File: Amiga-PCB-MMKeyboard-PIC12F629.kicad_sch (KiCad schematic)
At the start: 10 parts, among them J11 Amiga keyboard connector, J12 A500 keyboard connector, J2 PS/2 keyboard connector, U1 PIC12F629-IP

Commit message: v02
- Update PS/2 socket footprint
- Print "values" on silkscreen
- Add 100 nF for PIC
- Shorten "values"
- Move things to the left for more space and to balance the look
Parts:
- added C1: 100nF, Capacitor_SMD:C_0805_2012Metric_Pad1.18x1.45mm_HandSolder, symbol Device:C
- D1: footprint LED_SMD:LED_0805_2012Metric -> LED_SMD:LED_0805_2012Metric_Pad1.15x1.40mm_HandSolder
- D2: value Floppy 0805 -> Drive 0805; footprint LED_SMD:LED_0805_2012Metric -> LED_SMD:LED_0805_2012Metric_Pad1.15x1.40mm_HandSolder
- D3: value Power 2.54 -> Power
- D4: value Floppy 2.54 -> Drive
- J11: value Amiga keyboard connector -> Amiga keyboard
- J12: value A500 keyboard connector -> A500 mainboard
- J2: value PS/2 keyboard connector -> PS/2 keyboard
- R1, R2: footprint Resistor_SMD:R_0805_2012Metric -> Resistor_SMD:R_0805_2012Metric_Pad1.20x1.40mm_HandSolder
- U1: value PIC12F629-IP -> PIC12F629
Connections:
- net GND: now also C1.2
- net VCC: now also C1.1
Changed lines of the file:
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@@
+    )
+  )
+  (global_label "VCC" (shape input) (at 233.68 29.21 180) (fields_autoplaced)
+    (effects (font (size 1.27 1.27)) (justify right))
+    (property "Intersheetrefs" "${INTERSHEET_REFS}" (at 227.0662 29.21 0)
+      (effects (font (size 1.27 1.27)) (justify right) hide)
     )
   )
@@
       (effects (font (size 1.27 1.27)))
     )
-    (property "Value" "Amiga keyboard connector" (at 116.8577 28.7599 0)
+    (property "Value" "Amiga keyboard" (at 116.8577 28.7599 0)
       (effects (font (size 1.27 1.27)))
     )
@@
       (effects (font (size 1.27 1.27)))
     )
-    (property "Value" "PS/2 keyboard connector" (at 204.4877 69.3999 0)
+    (property "Value" "PS/2 keyboard" (at 204.4877 69.3999 0)
       (effects (font (size 1.27 1.27)))
     )
@@
       (effects (font (size 1.27 1.27)))
     )
-    (property "Footprint" "Resistor_SMD:R_0805_2012Metric" (at 144.78 97.028 90)
+    (property "Footprint" "Resistor_SMD:R_0805_2012Metric_Pad1.20x1.40mm_HandSolder" (at 144.78 97.028 90)
       (effects (font (size 1.27 1.27)) hide)
     )
@@
       (effects (font (size 1.27 1.27)) (justify left))
     )
-    (property "Value" "PIC12F629-IP" (at 181.2641 30.0299 0)
+    (property "Value" "PIC12F629" (at 181.2641 30.0299 0)
       (effects (font (size 1.27 1.27)) (justify left))
     )
@@
       (effects (font (size 1.27 1.27)))
     )
-    (property "Value" "Power 2.54" (at 174.3075 86.2909 0)
+    (property "Value" "Power" (at 174.3075 86.2909 0)
       (effects (font (size 1.27 1.27)))
     )
@@
       (effects (font (size 1.27 1.27)))
     )
-    (property "Value" "Floppy 0805" (at 153.9875 91.3709 0)
-      (effects (font (size 1.27 1.27)))
-    )
-    (property "Footprint" "LED_SMD:LED_0805_2012Metric" (at 152.4 95.25 0)
+    (property "Value" "Drive 0805" (at 153.9875 91.3709 0)
+      (effects (font (size 1.27 1.27)))
+    )
+    (property "Footprint" "LED_SMD:LED_0805_2012Metric_Pad1.15x1.40mm_HandSolder" (at 152.4 95.25 0)
       (effects (font (size 1.27 1.27)) hide)
     )
@@
       (effects (font (size 1.27 1.27)))
     )
-    (property "Value" "Floppy 2.54" (at 153.9875 104.0709 0)
+    (property "Value" "Drive" (at 153.9875 104.0709 0)
       (effects (font (size 1.27 1.27)))
     )
@@
     )
   )
+  (symbol (lib_id "Device:C") (at 237.49 29.21 90) (unit 1)
+    (in_bom yes) (on_board yes) (dnp no) (fields_autoplaced)
+    (property "Reference" "C1" (at 237.49 22.9067 90)
+      (effects (font (size 1.27 1.27)))
+    )
+    (property "Value" "100nF" (at 237.49 25.3309 90)
+      (effects (font (size 1.27 1.27)))
+    )
+    (property "Footprint" "Capacitor_SMD:C_0805_2012Metric_Pad1.18x1.45mm_HandSolder" (at 241.3 28.2448 0)
+      (effects (font (size 1.27 1.27)) hide)
+    )
+    (property "Datasheet" "~" (at 237.49 29.21 0)
+      (effects (font (size 1.27 1.27)) hide)
+    )
+    (property "JLCPCB" "C49678" (at 237.49 29.21 90)
+      (effects (font (size 1.27 1.27)) hide)
+    )
+    (pin "2")
+    (pin "1")
+    (instances
+      (project "Amiga-PCB-MMKeyboard-PIC12F629"
+        (path "/0d18a371-b76e-400e-8049-12c2c408a5eb"
+          (reference "C1") (unit 1)
+        )
+      )
+    )
+  )
   (symbol (lib_id "Device:R") (at 165.1 77.47 90) (unit 1)
     (in_bom yes) (on_board yes) (dnp no) (fields_autoplaced)
@@
       (effects (font (size 1.27 1.27)))
     )
-    (property "Footprint" "Resistor_SMD:R_0805_2012Metric" (at 165.1 79.248 90)
+    (property "Footprint" "Resistor_SMD:R_0805_2012Metric_Pad1.20x1.40mm_HandSolder" (at 165.1 79.248 90)
       (effects (font (size 1.27 1.27)) hide)
     )
@@
   (symbol (lib_id "Connector:Conn_01x08_Socket") (at 129.54 63.5 0) (unit 1)
     (in_bom yes) (on_board yes) (dnp no) (fields_autoplaced)
-    (property "Reference" "J12" (at 133.6335 64.77 90)
-      (effects (font (size 1.27 1.27)))
-    )
-    (property "Value" "A500 keyboard connector" (at 131.2093 64.77 90)
-      (effects (font (size 1.27 1.27)))
+    (property "Reference" "J12" (at 130.2512 63.5579 0)
+      (effects (font (size 1.27 1.27)) (justify left))
+    )
+    (property "Value" "A500 mainboard" (at 130.2512 65.9821 0)
+      (effects (font (size 1.27 1.27)) (justify left))
     )
     (property "Footprint" "Connector_PinSocket_2.54mm:PinSocket_1x08_P2.54mm_Vertical" (at 129.54 63.5 0)
@@
     )
   )
+  (symbol (lib_id "power:GND") (at 241.3 29.21 0) (unit 1)
+    (in_bom yes) (on_board yes) (dnp no) (fields_autoplaced)
+    (property "Reference" "#PWR09" (at 241.3 35.56 0)
+      (effects (font (size 1.27 1.27)) hide)
+    )
+    (property "Value" "GND" (at 241.3 33.3431 0)
+      (effects (font (size 1.27 1.27)))
+    )
+    (property "Footprint" "" (at 241.3 29.21 0)
+      (effects (font (size 1.27 1.27)) hide)
+    )
+    (property "Datasheet" "" (at 241.3 29.21 0)
+      (effects (font (size 1.27 1.27)) hide)
+    )
+    (pin "1")
+    (instances
+      (project "Amiga-PCB-MMKeyboard-PIC12F629"
+        (path "/0d18a371-b76e-400e-8049-12c2c408a5eb"
+          (reference "#PWR09") (unit 1)
+        )
+      )
+    )
+  )
   (symbol (lib_id "Device:LED") (at 172.72 77.47 180) (unit 1)
     (in_bom yes) (on_board yes) (dnp no) (fields_autoplaced)
@@
       (effects (font (size 1.27 1.27)))
     )
-    (property "Footprint" "LED_SMD:LED_0805_2012Metric" (at 172.72 77.47 0)
-      (effects (font (size 1.27 1.27)) hide)
-    )
+    (property "Footprint" "LED_SMD:LED_0805_2012Metric_Pad1.15x1.40mm_HandSolder" (at 172.72 77.47 0)
+      (effects (font (size 1.27 1.27)) hide)
+    )

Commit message: v04: Change resistors to 470 Ohm, late A500 LED colours
200 Ohm are the original value seen on an A500 keyboard, but with modern
0805 LEDs this ends up too bright.

The JLCPCB/LCSC part numbers for the SMD LEDs are now:
 - Power: green
 - Drive: yellow
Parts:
- D1: JLCPCB C84256 -> C2297
- D2: JLCPCB C2297 -> C2296
- R1, R2: value 200 -> 470; JLCPCB C17540 -> C17710
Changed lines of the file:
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@@
       (effects (font (size 1.27 1.27)))
     )
-    (property "Value" "200" (at 144.78 92.5139 90)
+    (property "Value" "470" (at 144.78 92.5139 90)
       (effects (font (size 1.27 1.27)))
     )
@@
       (effects (font (size 1.27 1.27)) hide)
     )
-    (property "JLCPCB" "C17540" (at 144.78 95.25 0)
+    (property "JLCPCB" "C17710" (at 144.78 95.25 0)
       (effects (font (size 1.27 1.27)) hide)
     )
@@
       (effects (font (size 1.27 1.27)) hide)
     )
-    (property "JLCPCB" "C2297" (at 152.4 95.25 0)
+    (property "JLCPCB" "C2296" (at 152.4 95.25 0)
       (effects (font (size 1.27 1.27)) hide)
     )
@@
       (effects (font (size 1.27 1.27)))
     )
-    (property "Value" "200" (at 165.1 74.7339 90)
+    (property "Value" "470" (at 165.1 74.7339 90)
       (effects (font (size 1.27 1.27)))
     )
@@
       (effects (font (size 1.27 1.27)) hide)
     )
-    (property "JLCPCB" "C17540" (at 165.1 77.47 0)
+    (property "JLCPCB" "C17710" (at 165.1 77.47 0)
       (effects (font (size 1.27 1.27)) hide)
     )
@@
       (effects (font (size 1.27 1.27)) hide)
     )
-    (property "JLCPCB" "C84256" (at 172.72 77.47 0)
-      (effects (font (size 1.27 1.27)) hide)
-    )
+    (property "JLCPCB" "C2297" (at 172.72 77.47 0)
+      (effects (font (size 1.27 1.27)) hide)
+    )

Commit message: Add Reichelt order numbers
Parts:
- C1: Reichelt (none) -> KEM X7R0805 100N
- D1: Reichelt (none) -> LG R971
- D2: Reichelt (none) -> LY R976
- J11, J2: Reichelt (none) -> EB-DIOS M06V
- J12: Reichelt (none) -> MPE 094-1-008
- R1, R2: Reichelt (none) -> SMD-0805 470
- U1: Reichelt (none) -> PIC 12F629-I/P
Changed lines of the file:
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@@
+      (effects (font (size 1.27 1.27)) hide)
+    )
+    (property "Reichelt" "EB-DIOS M06V" (at 116.84 35.56 0)
       (effects (font (size 1.27 1.27)) hide)
     )
@@
       (effects (font (size 1.27 1.27)) hide)
     )
+    (property "Reichelt" "EB-DIOS M06V" (at 204.47 76.2 0)
+      (effects (font (size 1.27 1.27)) hide)
+    )
     (pin "4")
     (pin "6")
@@
       (effects (font (size 1.27 1.27)) hide)
     )
+    (property "Reichelt" "SMD-0805 470" (at 144.78 95.25 0)
+      (effects (font (size 1.27 1.27)) hide)
+    )
     (pin "1")
     (pin "2")
@@
     )
     (property "LCSC" "C72124" (at 179.07 41.91 0)
+      (effects (font (size 1.27 1.27)) hide)
+    )
+    (property "Reichelt" "PIC 12F629-I/P" (at 179.07 41.91 0)
       (effects (font (size 1.27 1.27)) hide)
     )
@@
       (effects (font (size 1.27 1.27)) hide)
     )
+    (property "Reichelt" "" (at 172.72 90.17 0)
+      (effects (font (size 1.27 1.27)) hide)
+    )
     (pin "1")
     (pin "2")
@@
       (effects (font (size 1.27 1.27)) hide)
     )
+    (property "Reichelt" "LY R976" (at 152.4 95.25 0)
+      (effects (font (size 1.27 1.27)) hide)
+    )
     (pin "1")
     (pin "2")
@@
       (effects (font (size 1.27 1.27)) hide)
     )
+    (property "Reichelt" "" (at 152.4 107.95 0)
+      (effects (font (size 1.27 1.27)) hide)
+    )
     (pin "1")
     (pin "2")
@@
       (effects (font (size 1.27 1.27)) hide)
     )
+    (property "Reichelt" "KEM X7R0805 100N" (at 237.49 29.21 0)
+      (effects (font (size 1.27 1.27)) hide)
+    )
     (pin "2")
     (pin "1")
@@
     )
     (property "LCSC" "" (at 165.1 77.47 0)
+      (effects (font (size 1.27 1.27)) hide)
+    )
+    (property "Reichelt" "SMD-0805 470" (at 165.1 77.47 0)
       (effects (font (size 1.27 1.27)) hide)
     )
@@
     )
     (property "LCSC" "C2685213" (at 129.54 63.5 0)
+      (effects (font (size 1.27 1.27)) hide)
+    )
+    (property "Reichelt" "MPE 094-1-008" (at 129.54 63.5 0)
       (effects (font (size 1.27 1.27)) hide)
     )
@@
       (effects (font (size 1.27 1.27)) hide)
     )
+    (property "Reichelt" "LG R971" (at 172.72 77.47 0)
+      (effects (font (size 1.27 1.27)) hide)
+    )

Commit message: v05: Fix A500 interface, add A500 reset button
The A500 part was untested.
 - data/clock were swapped
 - reset was wrongly connected to the PIC

Added a jumper to reset an A500.
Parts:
- added R500: 470, Resistor_SMD:R_0805_2012Metric_Pad1.20x1.40mm_HandSolder, symbol Device:R
- added SW500: SW_Push, Connector_PinHeader_2.54mm:PinHeader_1x02_P2.54mm_Horizontal, symbol Switch:SW_Push
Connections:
- net GND: now also SW500.1
- net amigaclock: now also J12.1 (Pin_1); no longer J12.2 (Pin_2)
- net amigadat: now also J12.2 (Pin_2); no longer J12.1 (Pin_1)
- net reset renamed reset2000
- net reset2000: no longer J12.3 (Pin_3)
- new net: R500.2, SW500.2
- new net reset500: J12.3 (Pin_3), R500.1
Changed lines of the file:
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@@
     )
   )
-  (global_label "reset" (shape input) (at 124.46 60.96 180) (fields_autoplaced)
-    (effects (font (size 1.27 1.27)) (justify right))
-    (property "Intersheetrefs" "${INTERSHEET_REFS}" (at 116.7576 60.96 0)
-      (effects (font (size 1.27 1.27)) (justify right) hide)
-    )
-  )
-  (global_label "amigadat" (shape input) (at 124.46 55.88 180) (fields_autoplaced)
-    (effects (font (size 1.27 1.27)) (justify right))
-    (property "Intersheetrefs" "${INTERSHEET_REFS}" (at 112.706 55.88 0)
+  (global_label "reset500" (shape input) (at 124.46 60.96 180) (fields_autoplaced)
+    (effects (font (size 1.27 1.27)) (justify right))
+    (property "Intersheetrefs" "${INTERSHEET_REFS}" (at 113.1291 60.96 0)
+      (effects (font (size 1.27 1.27)) (justify right) hide)
+    )
+  )
+  (global_label "amigadat" (shape input) (at 124.46 58.42 180) (fields_autoplaced)
+    (effects (font (size 1.27 1.27)) (justify right))
+    (property "Intersheetrefs" "${INTERSHEET_REFS}" (at 112.706 58.42 0)
       (effects (font (size 1.27 1.27)) (justify right) hide)
     )
@@
     )
   )
-  (global_label "reset" (shape input) (at 163.83 44.45 180) (fields_autoplaced)
-    (effects (font (size 1.27 1.27)) (justify right))
-    (property "Intersheetrefs" "${INTERSHEET_REFS}" (at 156.1276 44.45 0)
+  (global_label "reset2000" (shape input) (at 163.83 44.45 180) (fields_autoplaced)
+    (effects (font (size 1.27 1.27)) (justify right))
+    (property "Intersheetrefs" "${INTERSHEET_REFS}" (at 151.2896 44.45 0)
+      (effects (font (size 1.27 1.27)) (justify right) hide)
+    )
+  )
+  (global_label "reset500" (shape input) (at 199.39 109.22 180) (fields_autoplaced)
+    (effects (font (size 1.27 1.27)) (justify right))
+    (property "Intersheetrefs" "${INTERSHEET_REFS}" (at 188.0591 109.22 0)
       (effects (font (size 1.27 1.27)) (justify right) hide)
     )
@@
     )
   )
-  (global_label "amigaclock" (shape input) (at 124.46 58.42 180) (fields_autoplaced)
-    (effects (font (size 1.27 1.27)) (justify right))
-    (property "Intersheetrefs" "${INTERSHEET_REFS}" (at 110.7102 58.42 0)
+  (global_label "amigaclock" (shape input) (at 124.46 55.88 180) (fields_autoplaced)
+    (effects (font (size 1.27 1.27)) (justify right))
+    (property "Intersheetrefs" "${INTERSHEET_REFS}" (at 110.7102 55.88 0)
       (effects (font (size 1.27 1.27)) (justify right) hide)
     )
@@
     )
   )
+  (symbol (lib_id "Device:R") (at 203.2 109.22 90) (unit 1)
+    (in_bom yes) (on_board yes) (dnp no) (fields_autoplaced)
+    (property "Reference" "R500" (at 203.2 104.0597 90)
+      (effects (font (size 1.27 1.27)))
+    )
+    (property "Value" "470" (at 203.2 106.4839 90)
+      (effects (font (size 1.27 1.27)))
+    )
+    (property "Footprint" "Resistor_SMD:R_0805_2012Metric_Pad1.20x1.40mm_HandSolder" (at 203.2 110.998 90)
+      (effects (font (size 1.27 1.27)) hide)
+    )
+    (property "Datasheet" "~" (at 203.2 109.22 0)
+      (effects (font (size 1.27 1.27)) hide)
+    )
+    (property "JLCPCB" "C17710" (at 203.2 109.22 0)
+      (effects (font (size 1.27 1.27)) hide)
+    )
+    (property "LCSC" "" (at 203.2 109.22 0)
+      (effects (font (size 1.27 1.27)) hide)
+    )
+    (property "Reichelt" "SMD-0805 470" (at 203.2 109.22 0)
+      (effects (font (size 1.27 1.27)) hide)
+    )
+    (pin "1")
+    (pin "2")
+    (instances
+      (project "Amiga-PCB-MMKeyboard-PIC12F629"
+        (path "/0d18a371-b76e-400e-8049-12c2c408a5eb"
+          (reference "R500") (unit 1)
+        )
+      )
+    )
+  )
   (symbol (lib_id "power:GND") (at 139.7 35.56 0) (unit 1)
     (in_bom yes) (on_board yes) (dnp no) (fields_autoplaced)
@@
         (path "/0d18a371-b76e-400e-8049-12c2c408a5eb"
           (reference "D4") (unit 1)
+        )
+      )
+    )
+  )
+  (symbol (lib_id "power:GND") (at 217.17 109.22 0) (unit 1)
+    (in_bom yes) (on_board yes) (dnp no) (fields_autoplaced)
+    (property "Reference" "#PWR010" (at 217.17 115.57 0)
+      (effects (font (size 1.27 1.27)) hide)
+    )
+    (property "Value" "GND" (at 217.17 113.3531 0)
+      (effects (font (size 1.27 1.27)))
+    )
+    (property "Footprint" "" (at 217.17 109.22 0)
+      (effects (font (size 1.27 1.27)) hide)
+    )
+    (property "Datasheet" "" (at 217.17 109.22 0)
+      (effects (font (size 1.27 1.27)) hide)
+    )
+    (pin "1")
+    (instances
+      (project "Amiga-PCB-MMKeyboard-PIC12F629"
+        (path "/0d18a371-b76e-400e-8049-12c2c408a5eb"
+          (reference "#PWR010") (unit 1)
         )
       )
@@
         )
       )
+    )
+  )
+  (symbol (lib_id "Switch:SW_Push") (at 212.09 109.22 0) (mirror y) (unit 1)
+    (in_bom yes) (on_board yes) (dnp no)
+    (property "Reference" "SW500" (at 212.09 102.1547 0)
+      (effects (font (size 1.27 1.27)))
+    )
+    (property "Value" "SW_Push" (at 212.09 104.5789 0)
+      (effects (font (size 1.27 1.27)))
+    )
+    (property "Footprint" "Connector_PinHeader_2.54mm:PinHeader_1x02_P2.54mm_Horizontal" (at 212.09 104.14 0)
+      (effects (font (size 1.27 1.27)) hide)
+    )
+    (property "Datasheet" "~" (at 212.09 104.14 0)
+      (effects (font (size 1.27 1.27)) hide)
+    )
+    (property "LCSC" "C7501290" (at 212.09 109.22 0)
+      (effects (font (size 1.27 1.27)) hide)
+    )
+    (property "Reichelt" "W+P 946-142" (at 212.09 109.22 0)
+      (effects (font (size 1.27 1.27)) hide)
+    )
+    (pin "2")
+    (pin "1")
+    (instances
+      (project "Amiga-PCB-MMKeyboard-PIC12F629"
+        (path "/0d18a371-b76e-400e-8049-12c2c408a5eb"
+          (reference "SW500") (unit 1)
+        )
+      )

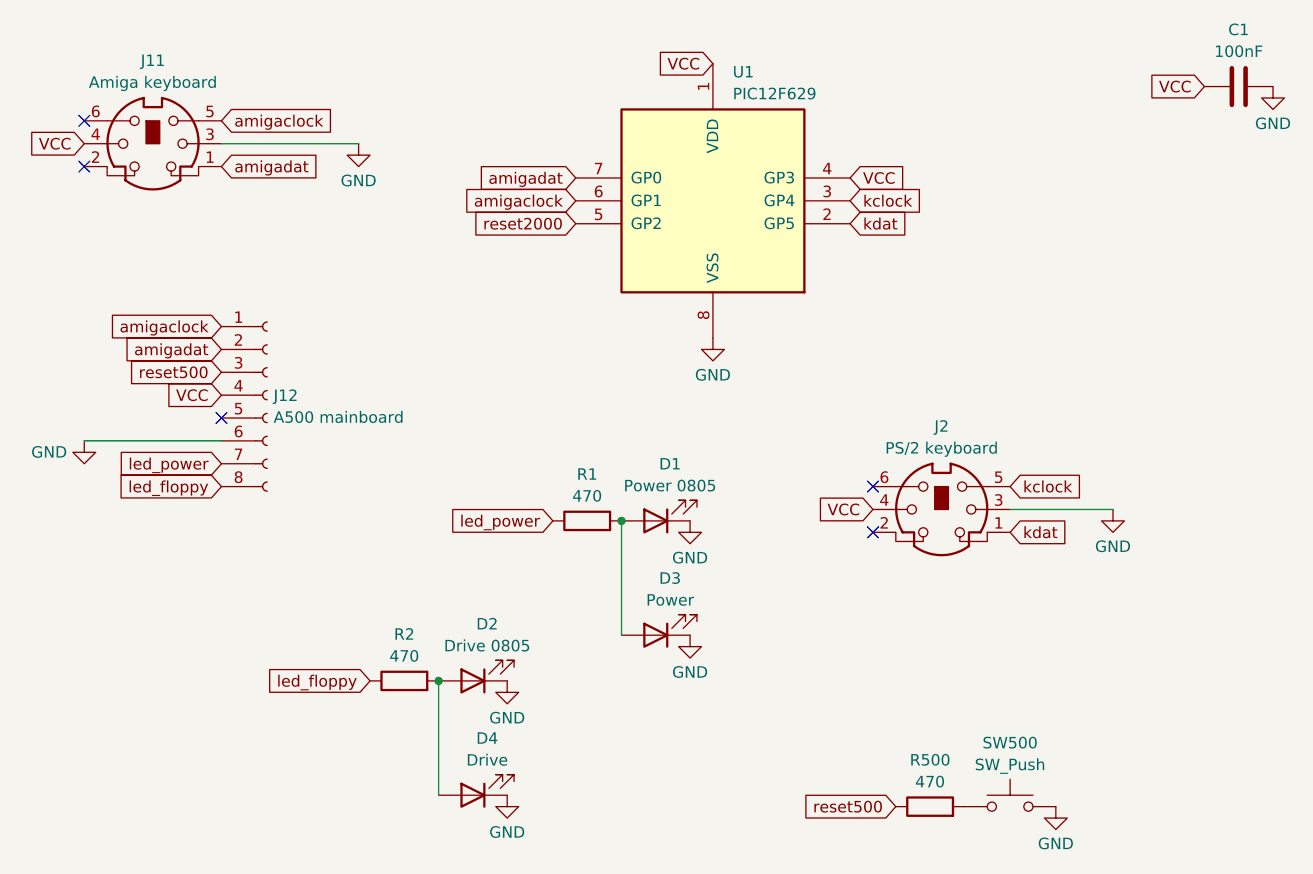
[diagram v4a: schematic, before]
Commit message: KiCad 9.0 and add local copy of Mini-DIN-6 socket footprint
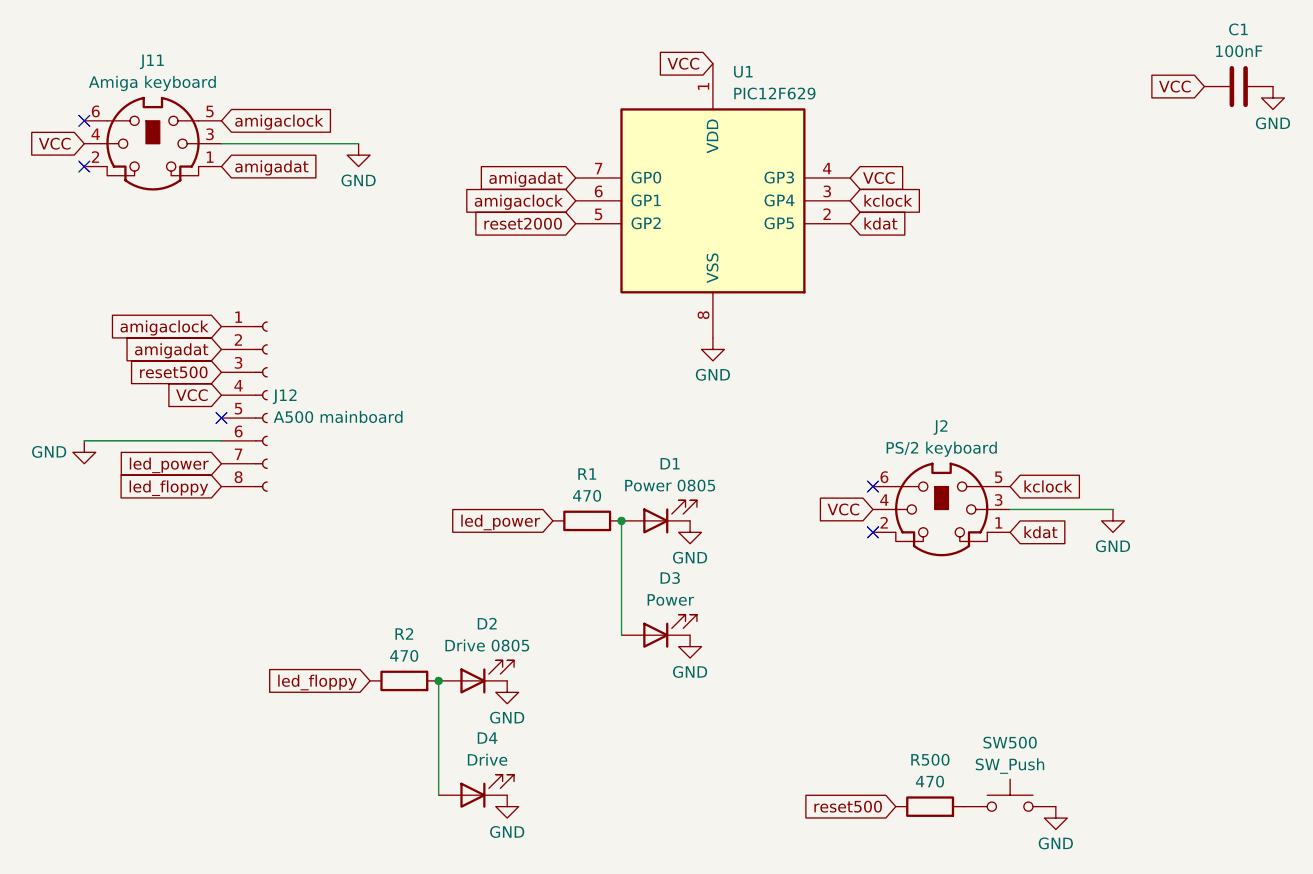
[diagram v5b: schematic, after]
